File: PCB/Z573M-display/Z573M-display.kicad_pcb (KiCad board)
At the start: 2 copper layers, 163.3 x 77.2 mm, 61 parts, among them J1 OSTVN02A150, J2 OSTVN02A150, J4 Conn_01x05_Socket, J5 Conn_01x06_Socket, Q1 MPSA92, Q10 MPSA42, Q11 MPSA42, Q12 MPSA42, Q13 MPSA42, Q2 MPSA92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

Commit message: Horizontal pins
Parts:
- added REF**: High_voltage_6.5mm, nixie-2.1-footprints:High_voltage_6.5mm, F.Cu at (73.0, 136.9)
- added REF**: High_Voltage_warning, nixie-2.1-footprints:High_Voltage_warning, F.Cu at (48.3, 88.9)
- added REF**: High_voltage_6.5mm, nixie-2.1-footprints:High_voltage_6.5mm, F.Cu at (124.0, 137.4)
- J4: footprint nixie-2.1-footprints:PinHeader_1x05_P2.54mm_Vertical -> Connector_PinHeader_2.54mm:PinHeader_1x05_P2.54mm_Horizontal
- J5: footprint nixie-2.1-footprints:PinHeader_1x06_P2.54mm_Vertical -> Connector_PinHeader_2.54mm:PinHeader_1x06_P2.54mm_Horizontal
- moved J5 12.7 mm to (132.8, 90.9), turned to 90 degrees
- moved J4 10.2 mm to (106.7, 90.9), turned to 90 degrees
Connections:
- J4 pad 1: A0 -> DP
- J4 pad 2: A1 -> A3
- J4 pad 4: A3 -> A1
- J4 pad 5: DP -> A0
- J5 pad 1: digit_0 -> digit_5
- J5 pad 2: digit_1 -> digit_4
- J5 pad 3: digit_2 -> digit_3
- J5 pad 4: digit_3 -> digit_2
- J5 pad 5: digit_4 -> digit_1
- J5 pad 6: digit_5 -> digit_0
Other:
- board text added: "200v"
- board text added: "5v"
- board text added: "A0"
- board text added: "A1"
- board text added: "A2"
- board text added: "A3"
- board text added: "DP"
- board text added: "Digit 0"
- board text added: "Digit 1"
- board text added: "Digit 2"
- board text added: "Digit 3"
- board text added: "Digit 4"
- board text added: "Digit 5"
- board text added: "GND"
- board text added: "locked"
- board text removed: "James gallager"
- board text removed: "Nixie 2.1 4/23/23 Version 0.1"

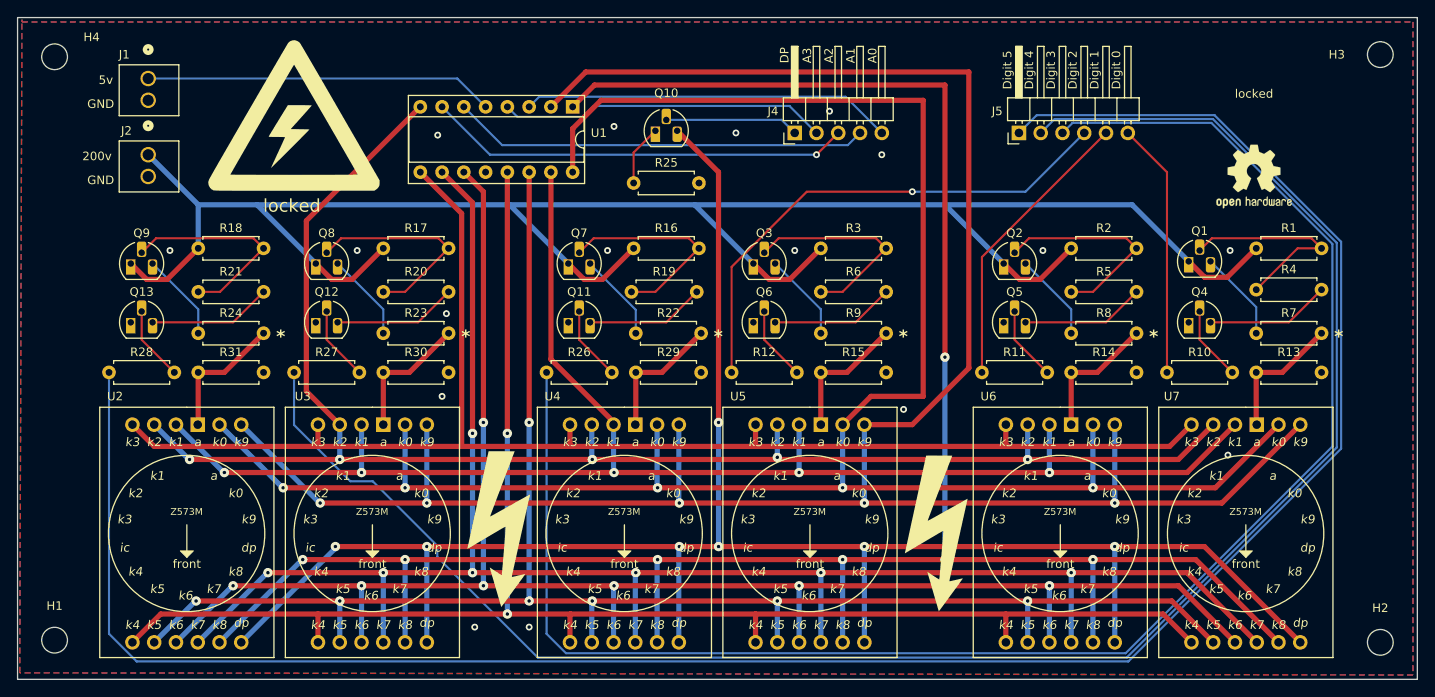
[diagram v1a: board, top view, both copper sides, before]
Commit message: Updated PCB with horizontal pin headers and better footprint silkscreens
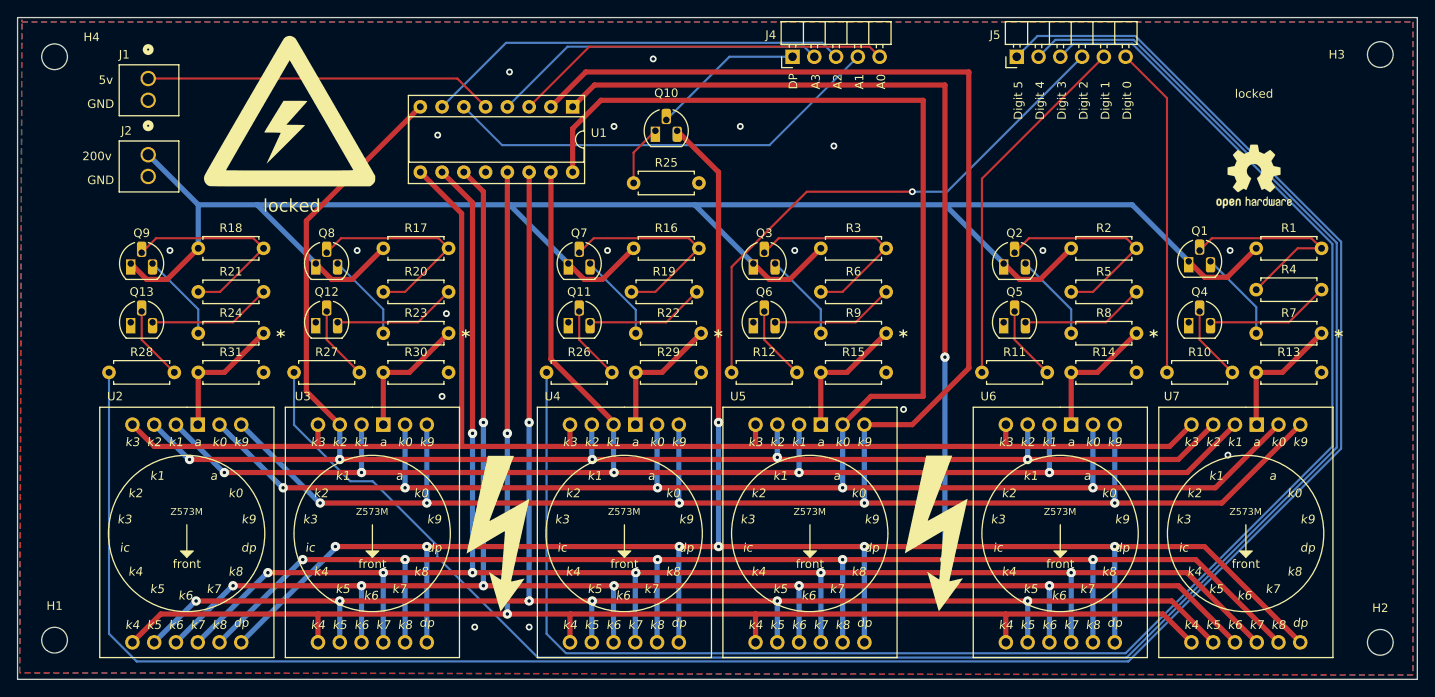
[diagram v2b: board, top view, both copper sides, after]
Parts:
- moved J4 8.89 mm to (106.4, 82.0)
- moved J5 8.89 mm to (132.6, 82.0)
- moved G*** 0.92 mm to (47.8, 89.2)
- moved REF** 0.72 mm to (47.8, 88.4)
- moved REF** 0.54 mm to (72.9, 137.4)
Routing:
- net digit_0: track 29.8 -> 38.8 mm
- net digit_1: track 33.9 -> 42.7 mm
- net digit_4: track 215.0 -> 219.3 mm
- net digit_3: track 194.6 -> 198.8 mm
- net digit_5: track 254.6 -> 258.8 mm
- net A1: track 48.7 -> 52.1 mm
- net digit_2: track 59.9 -> 63.4 mm
- net DP: track 15.6 -> 17.8 mm
- net A0: track 43.4 -> 44.3 mm
- net A3: track 38.4 -> 39.2 mm
- net A2: track 49.6 -> 49.7 mm, vias 1 -> 0
- net GND: vias 18 -> 19

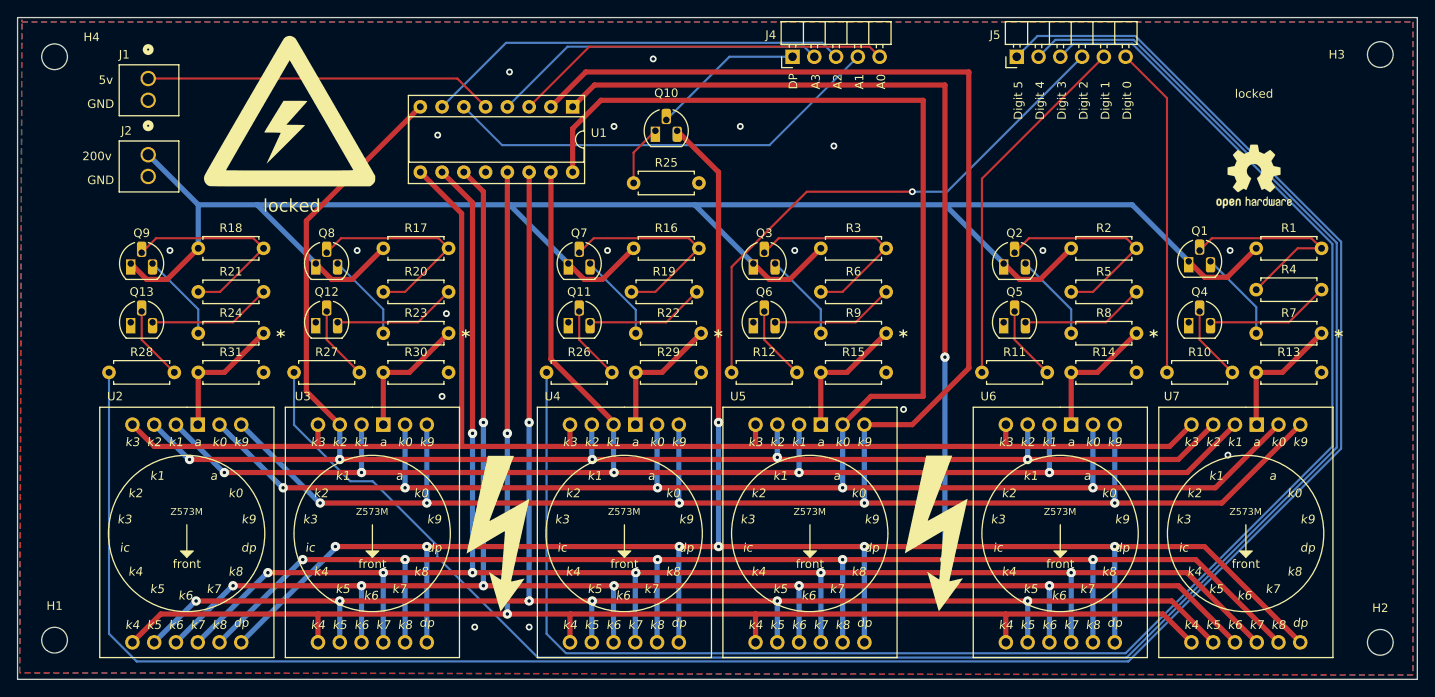
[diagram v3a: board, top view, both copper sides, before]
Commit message: Display and logic board edits
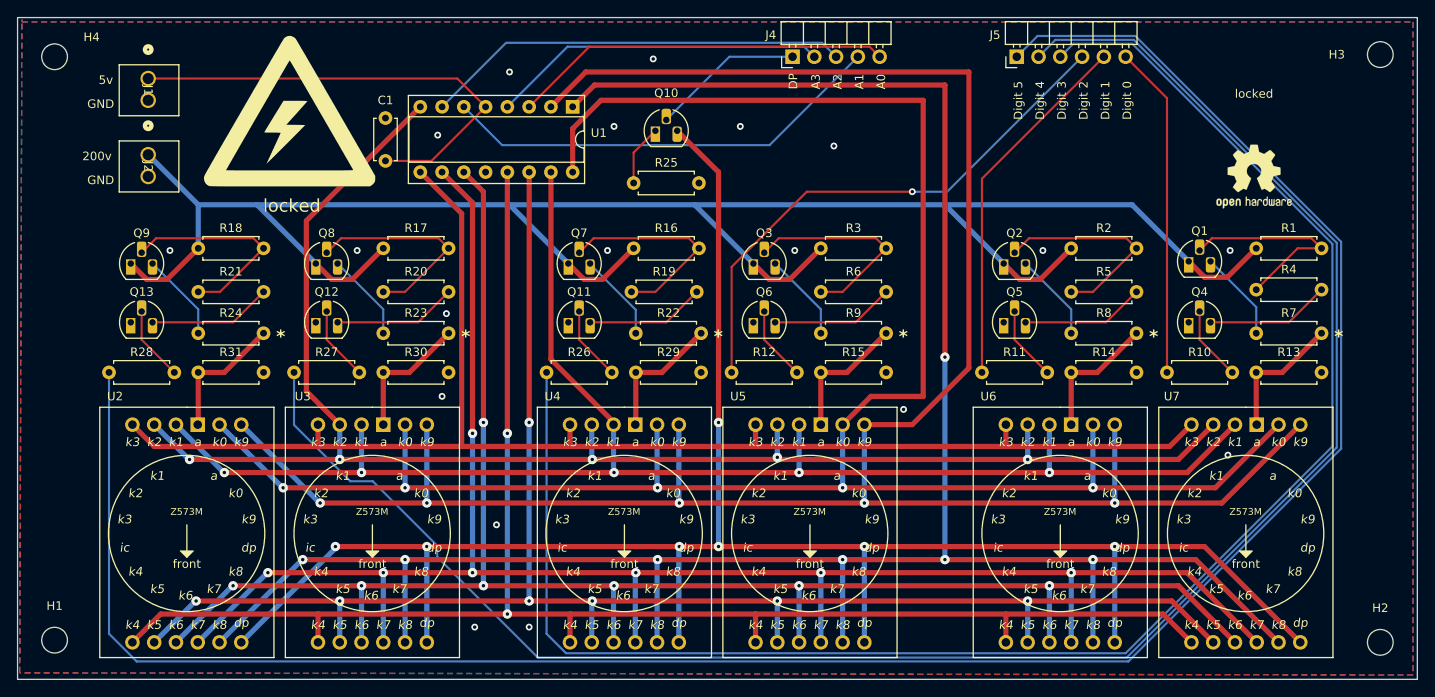
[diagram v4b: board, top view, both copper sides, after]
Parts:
- removed the REF** at (72.9, 137.4)
- removed the REF** at (124.0, 137.4)
- added C1: 100nF, Capacitor_THT:C_Disc_D4.7mm_W2.5mm_P5.00mm, F.Cu at (58.9, 94.2)
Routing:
- net VCC: track 40.7 -> 55.0 mm
